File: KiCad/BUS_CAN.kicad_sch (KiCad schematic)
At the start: 0 parts

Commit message: BUS CAN + USART +GND comuns
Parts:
- added C2: 100n, symbol Device:C
- added J1: DE9_Pins_MountingHoles, symbol Connector:DE9_Pins_MountingHoles
- added R3: 10k, symbol Device:R
- added R4: 120, symbol Device:R
- added U6: SN65HVD230, Package_SO:SOIC-8_3.9x4.9mm_P1.27mm, symbol Interface_CAN_LIN:SN65HVD230
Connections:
- new net: R3.1, U6.8 (Rs)
- new net CANH: J1.3, R4.1, U6.7 (CANH)
- new net CANL: J1.7, R4.2, U6.6 (CANL)
- new net CANRX: U6.4 (R)
- new net CANTX: U6.1 (D)
- new net GND_PWR: C2.1, J1.1, R3.2, U6.2 (GND)
- new net RX: J1.9
- new net TX: J1.5
- new net VDD_3V3: C2.2, U6.3 (VCC)
- no-connect marks 0 -> 5
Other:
- note added: "Pin Rs --> Resistencia 10k per slope control. Slew rate = 15V/us"
- note added: "Pin Vref --> Output Vcc/2"

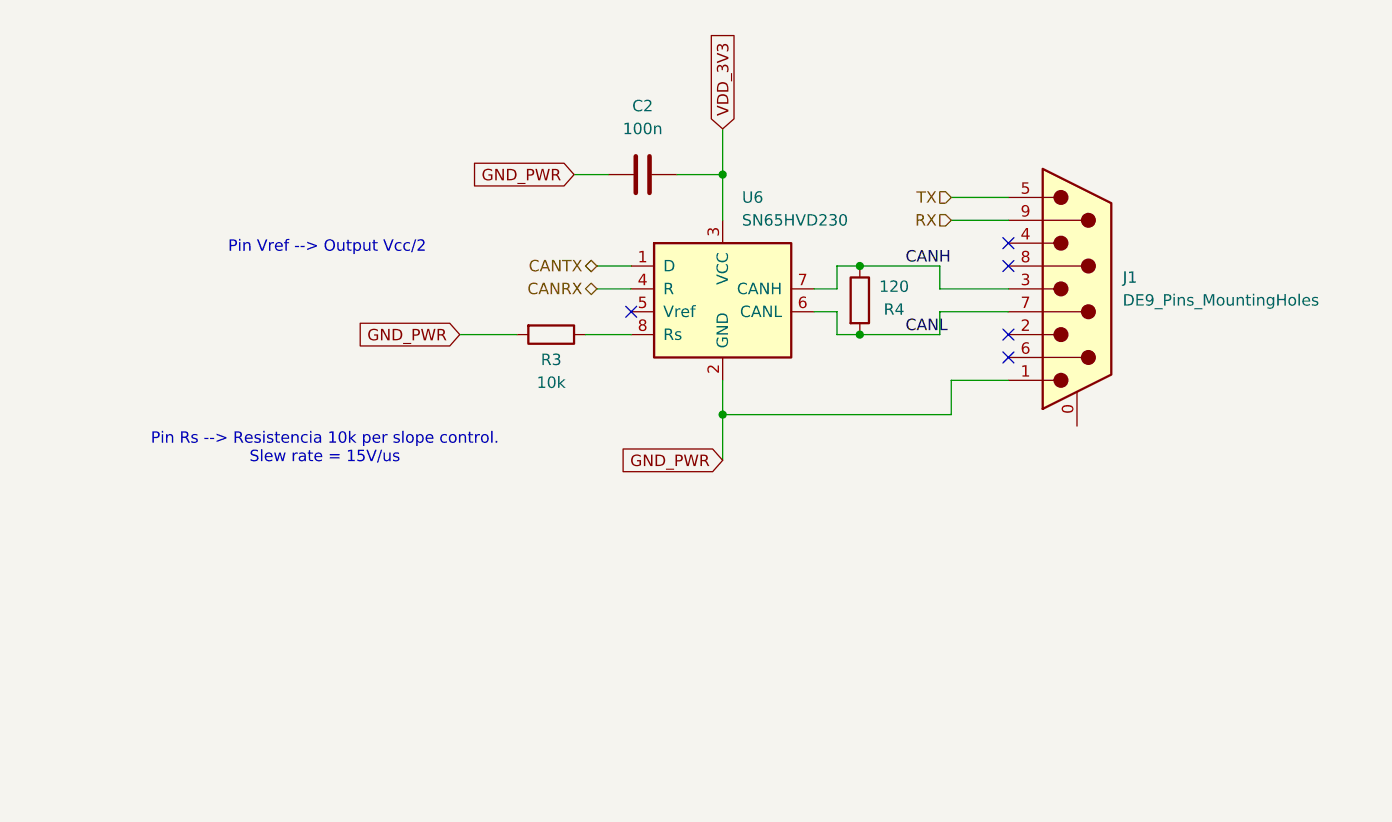
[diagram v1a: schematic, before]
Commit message: Diagrama blocs versió 4 + BOM actualitzat + Bus CAN i USART + Lector RFID
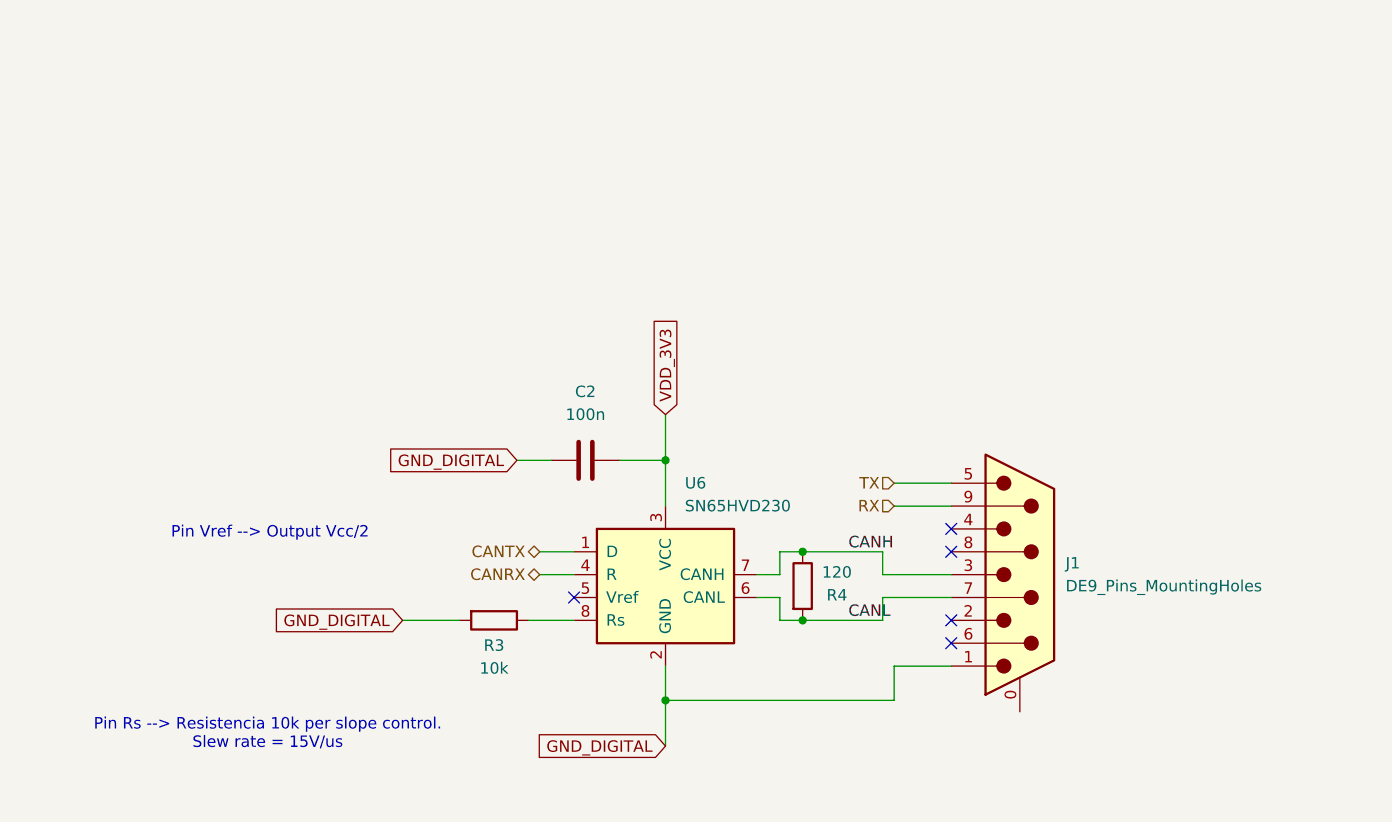
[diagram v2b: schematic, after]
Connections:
- net GND_PWR renamed GND_DIGITAL
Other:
- moved on the sheet: C2, J1, R3, R4, U6

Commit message: Footprints afegides a Comunicació, Sensor RFID i Sensor Corrent
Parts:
- C2: footprint (none) -> Capacitor_SMD:C_0805_2012Metric_Pad1.18x1.45mm_HandSolder
- J1: footprint (none) -> Connector_Dsub:DSUB-9_Socket_Vertical_P2.77x2.84mm_MountingHoles
- R3, R4: footprint (none) -> Resistor_SMD:R_0805_2012Metric_Pad1.20x1.40mm_HandSolder
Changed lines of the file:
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@@
 			)
 		)
-		(property "Footprint" ""
+		(property "Footprint" "Resistor_SMD:R_0805_2012Metric_Pad1.20x1.40mm_HandSolder"
 			(at 123.19 93.472 90)
 			(effects
@@
 			)
 		)
-		(property "Footprint" ""
+		(property "Footprint" "Capacitor_SMD:C_0805_2012Metric_Pad1.18x1.45mm_HandSolder"
 			(at 137.16 76.5048 0)
 			(effects
@@
 			)
 		)
-		(property "Footprint" ""
+		(property "Footprint" "Resistor_SMD:R_0805_2012Metric_Pad1.20x1.40mm_HandSolder"
 			(at 155.702 91.44 90)
 			(effects
@@
 			)
 		)
-		(property "Footprint" ""
+		(property "Footprint" "Connector_Dsub:DSUB-9_Socket_Vertical_P2.77x2.84mm_MountingHoles"
 			(at 181.61 90.17 0)
 			(effects

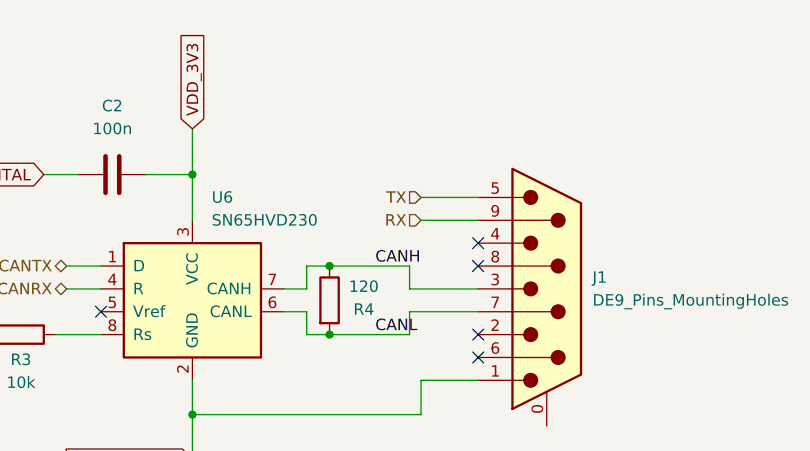
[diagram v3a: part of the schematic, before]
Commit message: Nova versió diagrama de blocs + BOM actualitzat + Nova versió KiCad
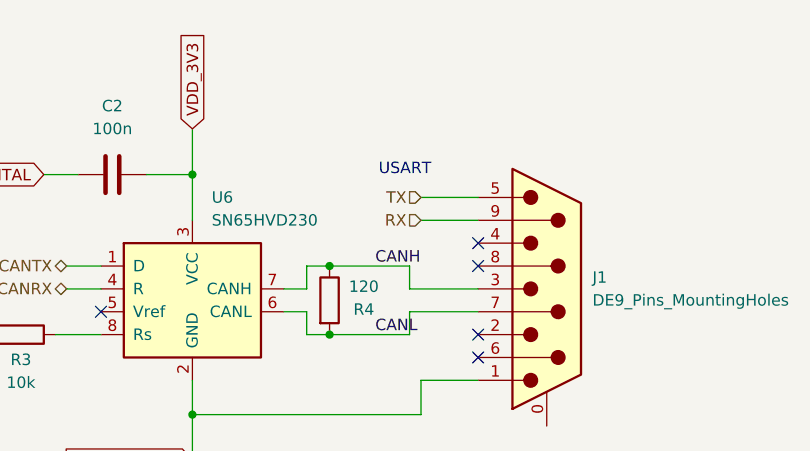
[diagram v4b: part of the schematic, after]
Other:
- note added: "USART"
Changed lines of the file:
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@@
+		)
+	)
+	(text "USART"
+		(exclude_from_sim no)
+		(at 165.862 76.962 0)
+		(effects
+			(font
+				(size 1.27 1.27)
+			)
 		)
 	)

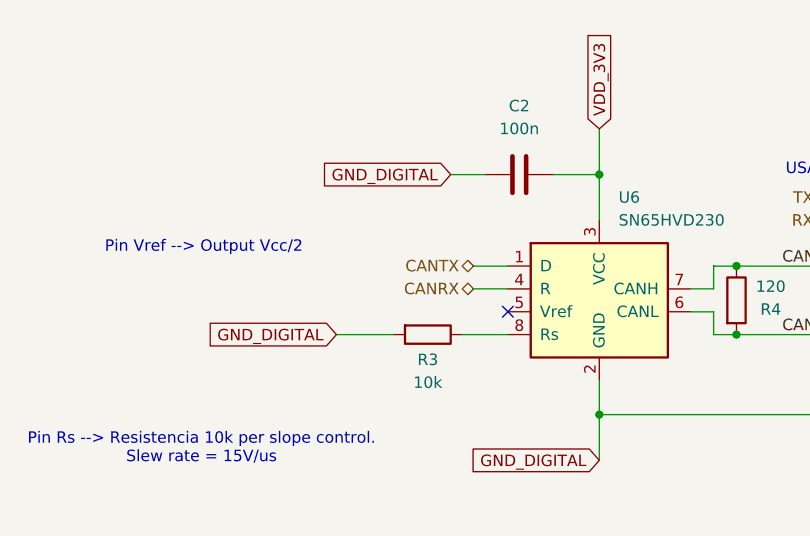
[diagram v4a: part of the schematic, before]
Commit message: Etiquetes de GND i VCC 3.3V canviades a simbols
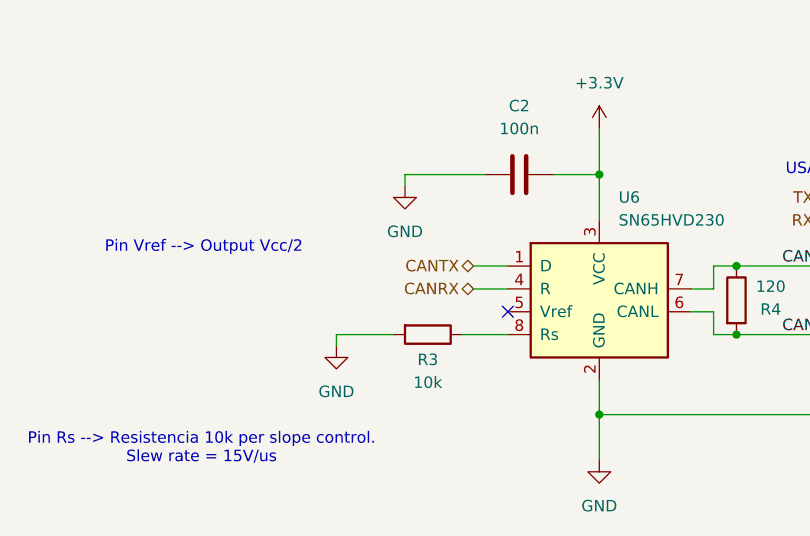
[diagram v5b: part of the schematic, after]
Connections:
- net GND_DIGITAL renamed GND
- net VDD_3V3 renamed +3.3V

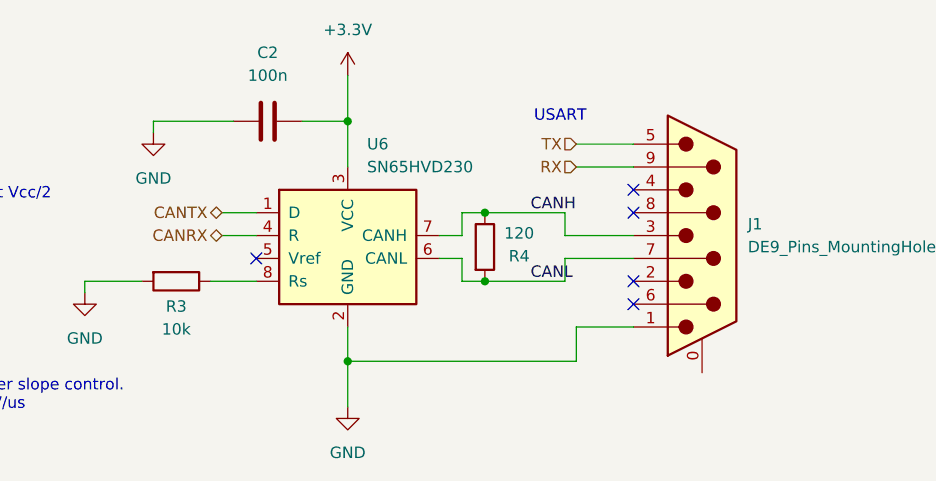
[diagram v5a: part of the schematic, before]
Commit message: Correció etapa d'alimentació e Inputs
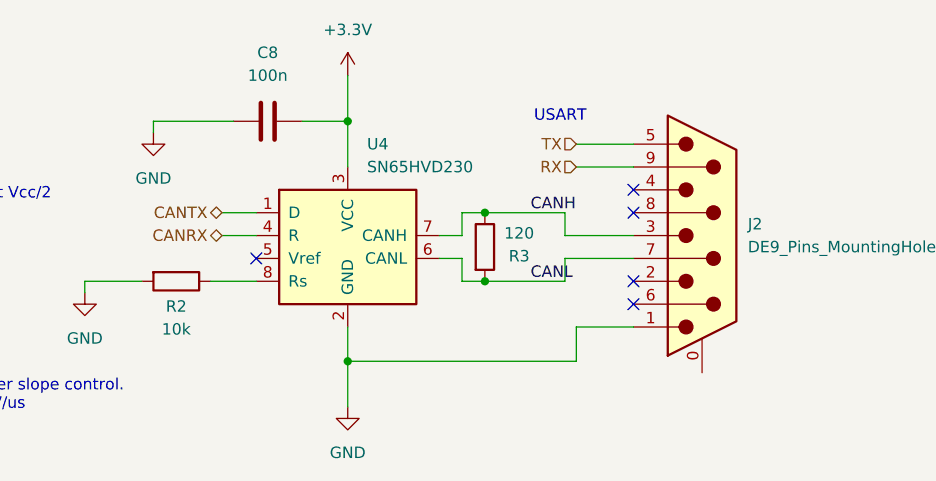
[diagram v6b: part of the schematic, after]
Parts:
- renumbered C2 to C8, J1 to J2, R3 to R2, R4 to R3, U6 to U4
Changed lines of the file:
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@@
 		(dnp no)
 		(fields_autoplaced yes)
-		(property "Reference" "#PWR015"
+		(property "Reference" "#PWR019"
 			(at 142.24 115.57 0)
 			(effects
@@
 			(project ""
 				(path "/347831db-5db9-4aff-ad32-e56fd770e219/119ce145-2c93-4544-b106-e85ec51fdc64"
-					(reference "#PWR015")
+					(reference "#PWR019")
 					(unit 1)
 				)
@@
 		(on_board yes)
 		(dnp no)
-		(property "Reference" "R3"
+		(property "Reference" "R2"
 			(at 123.19 98.044 90)
 			(effects
@@
 			(project ""
 				(path "/347831db-5db9-4aff-ad32-e56fd770e219/119ce145-2c93-4544-b106-e85ec51fdc64"
-					(reference "R3")
+					(reference "R2")
 					(unit 1)
 				)
@@
 		(dnp no)
 		(fields_autoplaced yes)
-		(property "Reference" "C2"
+		(property "Reference" "C8"
 			(at 133.35 69.85 90)
 			(effects
@@
 			(project ""
 				(path "/347831db-5db9-4aff-ad32-e56fd770e219/119ce145-2c93-4544-b106-e85ec51fdc64"
-					(reference "C2")
+					(reference "C8")
 					(unit 1)
 				)
@@
 		(on_board yes)
 		(dnp no)
-		(property "Reference" "R4"
+		(property "Reference" "R3"
 			(at 161.29 92.456 0)
 			(effects
@@
 			(project "PROJECTE_EINES"
 				(path "/347831db-5db9-4aff-ad32-e56fd770e219/119ce145-2c93-4544-b106-e85ec51fdc64"
-					(reference "R4")
+					(reference "R3")
 					(unit 1)
 				)
@@
 		(dnp no)
 		(fields_autoplaced yes)
-		(property "Reference" "J1"
+		(property "Reference" "J2"
 			(at 186.69 88.8999 0)
 			(effects
@@
 			(project ""
 				(path "/347831db-5db9-4aff-ad32-e56fd770e219/119ce145-2c93-4544-b106-e85ec51fdc64"
-					(reference "J1")
+					(reference "J2")
 					(unit 1)
 				)
@@
 		(dnp no)
 		(fields_autoplaced yes)
-		(property "Reference" "U6"
+		(property "Reference" "U4"
 			(at 144.3833 80.01 0)
 			(effects
@@
 			(project ""
 				(path "/347831db-5db9-4aff-ad32-e56fd770e219/119ce145-2c93-4544-b106-e85ec51fdc64"
-					(reference "U6")
-					(unit 1)
-				)
+					(reference "U4")
+					(unit 1)
+				)

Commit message: Versió final Esquematic
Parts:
- C8: footprint Capacitor_SMD:C_0805_2012Metric_Pad1.18x1.45mm_HandSolder -> Capacitor_SMD:C_0805_2012Metric
- R2, R3: footprint Resistor_SMD:R_0805_2012Metric_Pad1.20x1.40mm_HandSolder -> Resistor_SMD:R_0805_2012Metric
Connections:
- net CANRX renamed CAN_RX
- net CANTX renamed CAN_TX
- no-connect marks 5 -> 6
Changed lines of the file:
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@@
 		(at 173.99 95.25)
+	)
+	(no_connect
+		(at 181.61 105.41)
 	)
 	(wire
@@
 		)
 	)
-	(hierarchical_label "CANTX"
+	(hierarchical_label "CAN_TX"
 		(shape bidirectional)
 		(at 128.27 87.63 180)
@@
 		)
 	)
-	(hierarchical_label "CANRX"
+	(hierarchical_label "CAN_RX"
 		(shape bidirectional)
 		(at 128.27 90.17 180)
@@
 			)
 		)
-		(property "Footprint" "Resistor_SMD:R_0805_2012Metric_Pad1.20x1.40mm_HandSolder"
+		(property "Footprint" "Resistor_SMD:R_0805_2012Metric"
 			(at 123.19 93.472 90)
 			(effects
@@
 			)
 		)
-		(property "Footprint" "Capacitor_SMD:C_0805_2012Metric_Pad1.18x1.45mm_HandSolder"
+		(property "Footprint" "Capacitor_SMD:C_0805_2012Metric"
 			(at 137.16 76.5048 0)
 			(effects
@@
 			)
 		)
-		(property "Footprint" "Resistor_SMD:R_0805_2012Metric_Pad1.20x1.40mm_HandSolder"
+		(property "Footprint" "Resistor_SMD:R_0805_2012Metric"
 			(at 155.702 91.44 90)
 			(effects

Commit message: 1ra versióPCB
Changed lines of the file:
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@@
 		(on_board yes)
 		(dnp no)
-		(fields_autoplaced yes)
 		(property "Reference" "J2"
 			(at 186.69 88.8999 0)
@@
 		)
 		(property "Value" "DE9_Pins_MountingHoles"
-			(at 186.69 91.4399 0)
+			(at 186.69 91.44 0)
 			(effects
 				(font
